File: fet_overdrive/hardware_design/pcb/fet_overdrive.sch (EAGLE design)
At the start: 40 parts, among them IC1 TL072CD, J1 PJ301_THONKICONN6, J2 PJ301_THONKICONN6, Q1 MMBFJ111, Q2 SMMBT3904LT1G

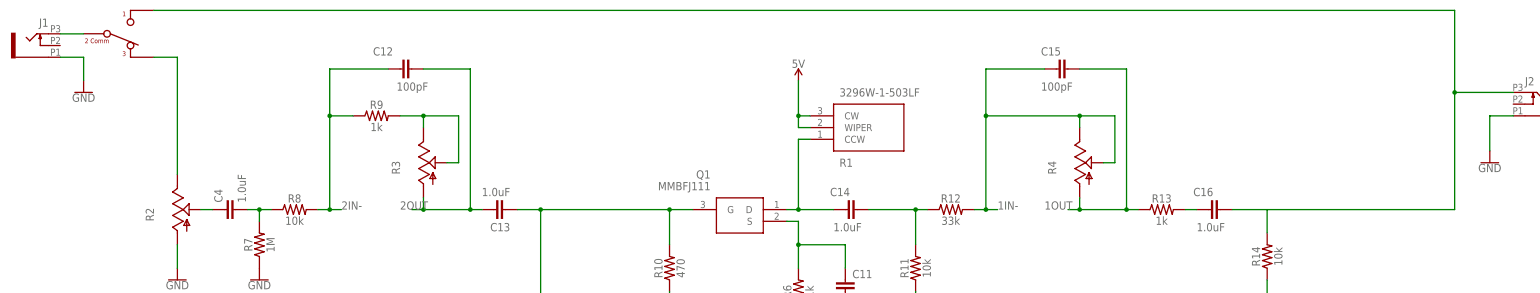
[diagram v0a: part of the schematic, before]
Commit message: design for fet overdrive and quantizer 2 code updates
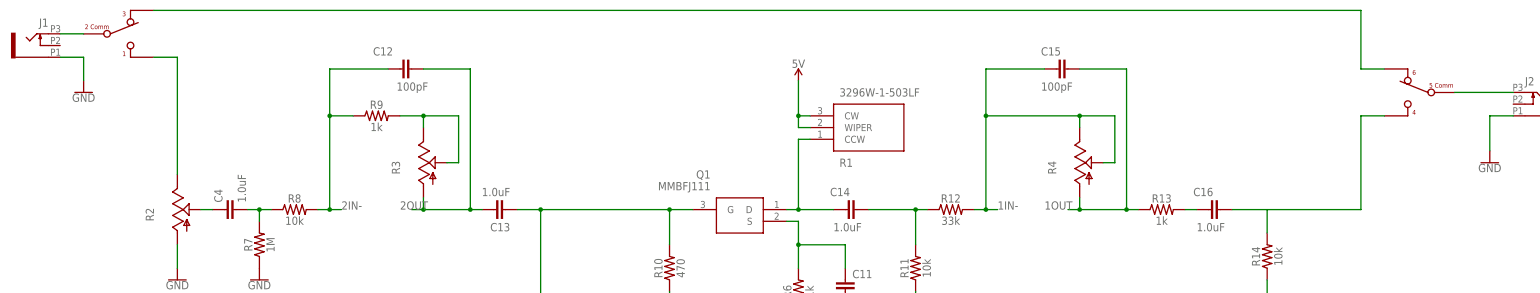
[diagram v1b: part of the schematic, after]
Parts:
- U$1: device Graphics v21:DAILYWELL -> Graphics v37:DAILYWELL-DPDT
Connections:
- new net N$1: C16.2, R14.2, U$1G$2.P$1
- new net N$17: J2.3, U$1G$2.P$2
- net N$15: now also U$1G$1.P$3, U$1G$2.P$3; no longer C16.2, J2.3, R14.2, U$1.P$1
- net N$2: now also U$1G$1.P$2; no longer U$1.P$2
- net N$6: now also U$1G$1.P$1; no longer U$1.P$3
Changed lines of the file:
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@@
 <part name="SUPPLY3" library="SparkFun-PowerSymbols" library_urn="urn:adsk.eagle:library:530" deviceset="5V" device=""/>
 <part name="Q1" library="MMBFJ111" deviceset="MMBFJ111" device=""/>
-<part name="U$1" library="Graphics v21" deviceset="DAILYWELL" device=""/>
 <part name="IC1" library="TL072CD" deviceset="TL072CD" device=""/>
 <part name="C1" library="EEE-FP1E220AR" deviceset="EEE-FP1E220AR" device=""/>
@@
 <part name="R14" library="SparkFun-Resistors" library_urn="urn:adsk.eagle:library:532" deviceset="10KOHM" device="-0603-1/10W-1%" package3d_urn="urn:adsk.eagle:package:39650/1" value="10k"/>
 <part name="GND16" library="SparkFun-PowerSymbols" library_urn="urn:adsk.eagle:library:530" deviceset="GND" device=""/>
+<part name="U$1" library="Graphics v37" deviceset="DAILYWELL-DPDT" device=""/>
 </parts>
 <sheets>
@@
 <attribute name="VALUE" x="179.07" y="185.42" size="1.778" layer="96" rot="MR0" align="center-left"/>
 </instance>
-<instance part="U$1" gate="G$1" x="53.34" y="218.44" smashed="yes"/>
 <instance part="IC1" gate="G$1" x="132.08" y="86.36" smashed="yes">
 <attribute name="NAME" x="156.21" y="93.98" size="1.778" layer="95" align="center-left"/>
@@
 <attribute name="VALUE" x="299.72" y="157.226" size="1.778" layer="96" align="top-center"/>
 </instance>
+<instance part="U$1" gate="G$1" x="53.34" y="218.44" smashed="yes" rot="MR180"/>
+<instance part="U$1" gate="G$2" x="330.2" y="205.74" smashed="yes" rot="R180"/>
 </instances>
 <busses>
@@
 <net name="N$6" class="0">
 <segment>
-<wire x1="58.42" y1="213.36" x2="63.5" y2="213.36" width="0.1524" layer="91"/>
-<pinref part="U$1" gate="G$1" pin="P$3"/>
 <wire x1="63.5" y1="213.36" x2="63.5" y2="187.96" width="0.1524" layer="91"/>
 <pinref part="R2" gate="G$1" pin="E"/>
+<wire x1="58.42" y1="213.36" x2="63.5" y2="213.36" width="0.1524" layer="91"/>
+<pinref part="U$1" gate="G$1" pin="P$1"/>
 </segment>
 </net>
@@
 <net name="N$15" class="0">
 <segment>
-<wire x1="58.42" y1="223.52" x2="340.36" y2="223.52" width="0.1524" layer="91"/>
-<wire x1="340.36" y1="223.52" x2="340.36" y2="205.74" width="0.1524" layer="91"/>
-<pinref part="J2" gate="G$1" pin="3"/>
-<wire x1="340.36" y1="205.74" x2="353.06" y2="205.74" width="0.1524" layer="91"/>
-<wire x1="340.36" y1="205.74" x2="340.36" y2="180.34" width="0.1524" layer="91"/>
-<junction x="340.36" y="205.74"/>
-<wire x1="340.36" y1="180.34" x2="299.72" y2="180.34" width="0.1524" layer="91"/>
-<pinref part="U$1" gate="G$1" pin="P$1"/>
-<wire x1="292.1" y1="180.34" x2="299.72" y2="180.34" width="0.1524" layer="91"/>
-<pinref part="C16" gate="G$1" pin="2"/>
-<wire x1="299.72" y1="180.34" x2="299.72" y2="175.26" width="0.1524" layer="91"/>
-<pinref part="R14" gate="G$1" pin="2"/>
+<wire x1="58.42" y1="223.52" x2="320.04" y2="223.52" width="0.1524" layer="91"/>
+<wire x1="320.04" y1="223.52" x2="320.04" y2="210.82" width="0.1524" layer="91"/>
+<wire x1="320.04" y1="210.82" x2="325.12" y2="210.82" width="0.1524" layer="91"/>
+<pinref part="U$1" gate="G$2" pin="P$3"/>
+<pinref part="U$1" gate="G$1" pin="P$3"/>
 </segment>
 </net>
@@
 </segment>
 </net>
+<net name="N$1" class="0">
+<segment>
+<pinref part="R14" gate="G$1" pin="2"/>
+<pinref part="C16" gate="G$1" pin="2"/>
+<wire x1="292.1" y1="180.34" x2="299.72" y2="180.34" width="0.1524" layer="91"/>
+<wire x1="299.72" y1="180.34" x2="299.72" y2="175.26" width="0.1524" layer="91"/>
+<wire x1="320.04" y1="180.34" x2="299.72" y2="180.34" width="0.1524" layer="91"/>
+<wire x1="325.12" y1="200.66" x2="320.04" y2="200.66" width="0.1524" layer="91"/>
+<wire x1="320.04" y1="200.66" x2="320.04" y2="180.34" width="0.1524" layer="91"/>
+<pinref part="U$1" gate="G$2" pin="P$1"/>
+</segment>
+</net>
+<net name="N$17" class="0">
+<segment>
+<pinref part="J2" gate="G$1" pin="3"/>
+<wire x1="340.36" y1="205.74" x2="353.06" y2="205.74" width="0.1524" layer="91"/>
+<pinref part="U$1" gate="G$2" pin="P$2"/>
+</segment>
+</net>
